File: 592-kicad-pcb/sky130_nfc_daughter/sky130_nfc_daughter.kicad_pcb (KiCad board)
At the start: 4 copper layers, 50 x 52 mm, 154 parts, among them J1 Conn_01x04, J10 U.FL, J11 U.FL, J12 U.FL, J13 U.FL, J2 U.FL, J3 U.FL, J4 U.FL, J5 U.FL, J6 U.FL, J7 U.FL, J8 U.FL, J9 U.FL, U1 Caravel_QFN, U2 24LC02, U3 W25Q32JVZP

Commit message: Add files via upload
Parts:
- removed J1: Conn_01x04, Connector_PinHeader_2.54mm:PinHeader_1x04_P2.54mm_Vertical
- removed J10, J11, J12, J13, J2, J3, J4, J5, J6, J7, J8, J9: U.FL, psysnapeda:SAMTEC_RSP-122811-01
- removed JP10, JP11, JP12, JP5, JP6, JP7, JP8, JP9: Jumper_2_Small_Bridged, Jumper:SolderJumper-2_P1.3mm_Bridged_RoundedPad1.0x1.5mm
- removed R1, R2: 1k, Resistor_SMD:R_0402_1005Metric
- removed R6, R7: 0R, Resistor_SMD:R_0402_1005Metric
- removed U2: 24LC02, Package_DFN_QFN:DFN-8-1EP_3x2mm_P0.5mm_EP1.75x1.45mm
- added JP13: Jumper_2_Small_Bridged, Jumper:SolderJumper-2_P1.3mm_Bridged_RoundedPad1.0x1.5mm, F.Cu at (81.3, 7.10)
- moved JP2 56.4 mm to (81.3, -3.55), turned to 0 degrees
- moved JP4 56.3 mm to (81.3, 3.55), turned to 0 degrees
- moved JP1 54.3 mm to (81.3, -7.10), turned to 0 degrees
- moved JP3 54.3 mm to (81.3, 0.00), turned to 0 degrees
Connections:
- net /hd_an0 renamed /J_ANA_MUX_OUT_EXT
- CON1 pad 36: /clock_uncore -> /J_clock_uncore
- CON1 pad 40: /VRECT_OUT_EXT -> /J_VRECT_OUT_EXT
- CON2 pad 20: /ext_clk_dig -> /J_ext_clk_dig
- CON2 pad 35: /ANA_MUX_OUT_2_EXT -> /J_ANA_MUX_OUT_2_EXT
- CON2 pad 38: /VREF_EXT -> /J_VREF_EXT
- CON2 pad 5: /clk -> /J_clk
- JP1 pad 1: /chip_an0 -> /ANA_MUX_OUT_EXT
- JP2 pad 1: /chip_an1 -> /ext_reset_dig
- JP2 pad 2: /hd_an1 -> /J_ext_clk_dig
- JP3 pad 1: /chip_an2 -> /clk
- JP3 pad 2: /hd_an2 -> /J_clk
- JP4 pad 1: /chip_an3 -> /clock_uncore
- JP4 pad 2: /hd_an3 -> /J_clock_uncore

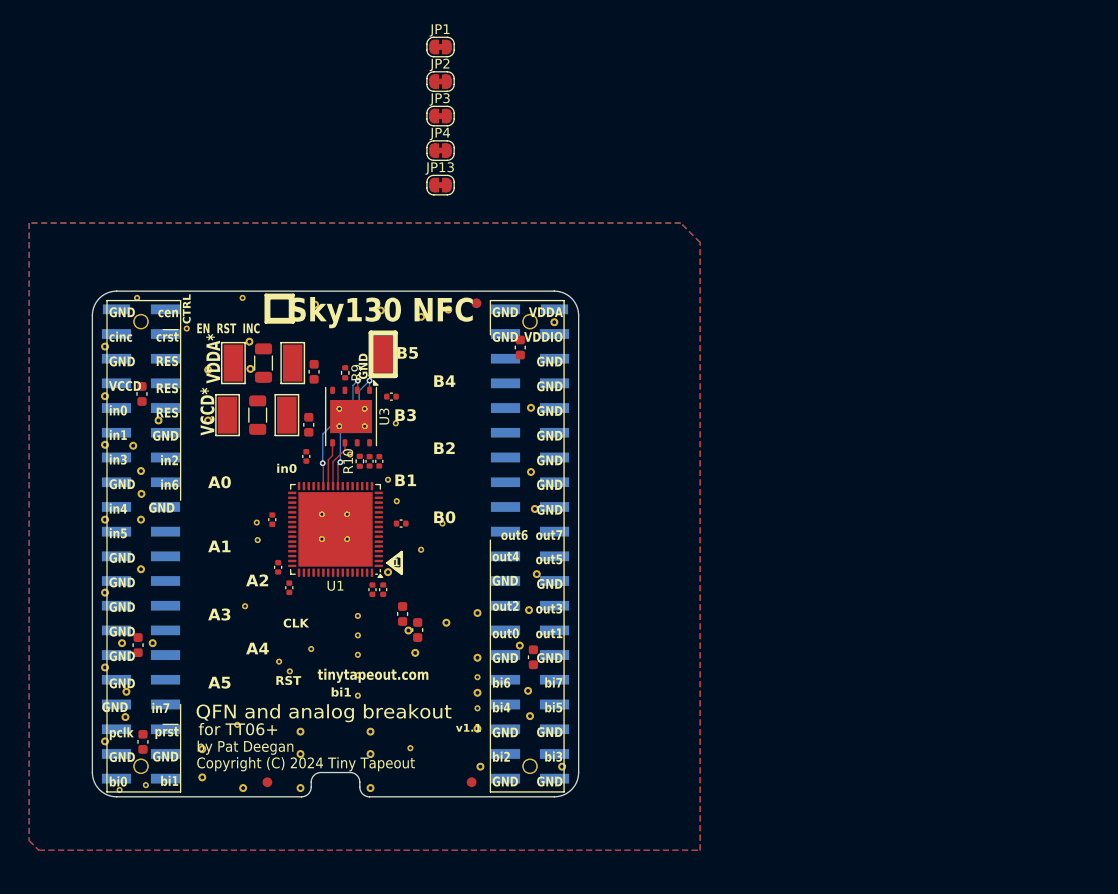
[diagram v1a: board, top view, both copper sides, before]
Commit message: add mezzanine symbol/footprint, init daughterboard placement
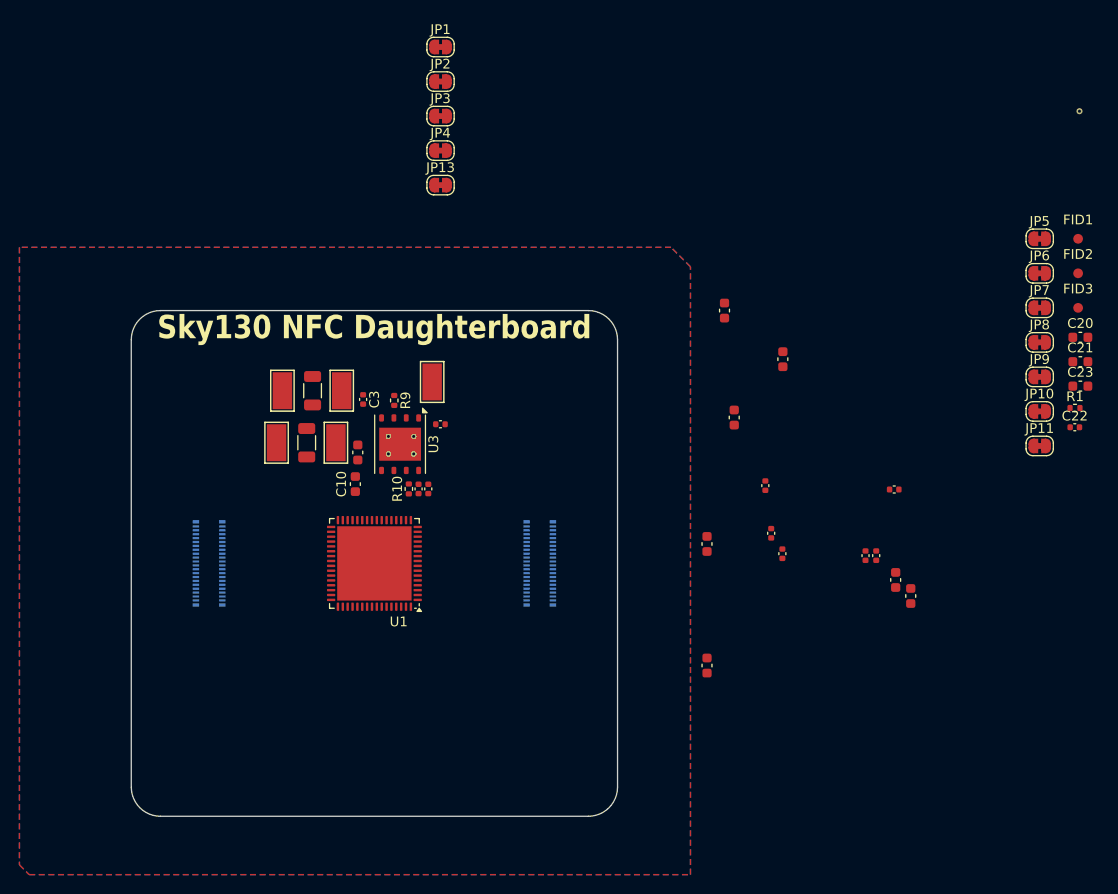
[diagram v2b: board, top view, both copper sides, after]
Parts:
- removed CON1, CON2: ~, TinyTapeout:FH-00148_PinSocket_2x20_P2.54mm
- removed REF**: Z2A_logo, Logos:Z2A_logo
- removed REF**: TT_logo, Logos:TT_logo
- removed STITCHB1 (x53): StitchingVia-0.4mmDrill, flyingcarsfootprints:StitchingVia-0.4mmDrill
- removed the STITCHM1 at (62.4, 41.8)
- removed the STITCHM1 at (78.2, 65.0)
- removed the STITCHM1 at (61.2, 50.4)
- removed the STITCHM1 at (72.8, 51.4)
- removed the STITCHM1 at (69.1, 41.0)
- removed the STITCHM1 at (64.7, 56.1)
- removed the STITCHM1 at (68.0, 54.8)
- removed the STITCHM1 at (55.2, 21.9)
- removed the STITCHM1 at (72.8, 55.4)
- removed the STITCHM1 at (76.8, 39.6)
- removed the STITCHM1 at (51.0, 68.8)
- removed the STITCHM1 at (60.4, 62.6)
- removed the STITCHM1 at (72.8, 53.4)
- removed the STITCHM1 at (65.8, 57.1)
- removed the STITCHM1 at (48.3, 69.3)
- removed the STITCHM1 at (81.5, 41.9)
- removed the STITCHM1 at (61.0, 18.7)
- removed the STITCHM1 at (71.7, 41.0)
- removed the STITCHM1 at (75.9, 37.4)
- removed the STITCHM1 at (62.5, 43.6)
- removed the STITCHM1 at (79.3, 44.6)
- removed the STITCHM1 at (85.1, 57.7)
- removed the STITCHM1 at (71.7, 43.5)
- removed the STITCHM1 at (50.1, 18.7)
- removed the STITCHM1 at (72.0, 34.8)
- removed the STITCHM1 at (72.8, 59.6)
- removed the STITCHM1 at (72.8, 57.5)
- removed the STITCHM1 at (85.1, 60.9)
- removed the STITCHM1 at (69.1, 43.5)
- added C20: C_1u_0603_50V, Capacitor_SMD:C_0603_1608Metric, F.Cu at (147.1, 22.8)
- added C21: C_1u_0603_50V, Capacitor_SMD:C_0603_1608Metric, F.Cu at (147.1, 25.3)
- added C22: 0.1uf, Capacitor_SMD:C_0402_1005Metric, F.Cu at (146.5, 32.0)
- added C23: C_1u_0603_50V, Capacitor_SMD:C_0603_1608Metric, F.Cu at (147.1, 27.8)
- added J8: DF40C-40DS-0.4V_51_, 592-partslib:DF40C40DP04V51, B.Cu at (57.5, 46.0)
- added J9: DF40C-40DS-0.4V_51_, 592-partslib:DF40C40DP04V51, B.Cu at (91.5, 46.0)
- added JP10: Jumper_2_Small_Bridged, Jumper:SolderJumper-2_P1.3mm_Bridged_RoundedPad1.0x1.5mm, F.Cu at (142.9, 30.4)
- added JP11: Jumper_2_Small_Bridged, Jumper:SolderJumper-2_P1.3mm_Bridged_RoundedPad1.0x1.5mm, F.Cu at (142.9, 33.9)
- added JP5: Jumper_2_Small_Bridged, Jumper:SolderJumper-2_P1.3mm_Bridged_RoundedPad1.0x1.5mm, F.Cu at (142.9, 12.6)
- added JP6: Jumper_2_Small_Bridged, Jumper:SolderJumper-2_P1.3mm_Bridged_RoundedPad1.0x1.5mm, F.Cu at (142.9, 16.2)
- added JP7: Jumper_2_Small_Bridged, Jumper:SolderJumper-2_P1.3mm_Bridged_RoundedPad1.0x1.5mm, F.Cu at (142.9, 19.7)
- added JP8: Jumper_2_Small_Bridged, Jumper:SolderJumper-2_P1.3mm_Bridged_RoundedPad1.0x1.5mm, F.Cu at (142.9, 23.3)
- added JP9: Jumper_2_Small_Bridged, Jumper:SolderJumper-2_P1.3mm_Bridged_RoundedPad1.0x1.5mm, F.Cu at (142.9, 26.8)
- added R1: 10k, Resistor_SMD:R_0402_1005Metric, F.Cu at (146.5, 30.0)
- C10: value 0.1uf -> C_1u_0603_50V; footprint Capacitor_SMD:C_0402_1005Metric -> Capacitor_SMD:C_0603_1608Metric
- C3: value C_1u_0603_50V -> 0.1uf; footprint Capacitor_SMD:C_0603_1608Metric -> Capacitor_SMD:C_0402_1005Metric
- moved FID1 100.4 mm to (146.9, 12.6)
- moved FID3 79.2 mm to (146.9, 19.7)
- moved STITCHM1 77.3 mm to (147.0, -0.50)
- moved FID2 61.9 mm to (146.9, 16.2)
- moved C15 60.5 mm to (110.5, 20.0)
- moved C17 59.4 mm to (108.7, 44.0)
- moved C14 58.5 mm to (108.7, 56.5)
- moved C11 50.8 mm to (114.7, 38.0)
- moved C12 50.8 mm to (115.3, 42.9)
- moved C13 50.8 mm to (128.0, 38.4)
- moved C18 50.8 mm to (129.7, 49.4)
- moved C4 50.8 mm to (116.5, 45.0)
- moved C5 50.8 mm to (125.0, 45.2)
- moved C19 50.8 mm to (128.1, 47.7)
- moved C8 50.8 mm to (126.1, 45.2)
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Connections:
- net Net-(U3-~{HOLD}/~{RESET}/IO_{3}) renamed /flash_rstb
- net Net-(U3-~{WP}/IO_{2}) renamed /flash_wpb
- C1 pad 1: vddio -> vddio_vdda_mgmt_3v3
- C10 pad 1: vdda_all -> vccd_mgmt_1v8
- C11 pad 1: vdda_all -> vdda_user_3v3
- C12 pad 1: vdda_all -> vdda_user_3v3
- C13 pad 2: vdda_all -> vdda_user_3v3
- C14 pad 1: vccd_all -> vccd_user_1v8
- C18 pad 1: vccd_all -> vccd_user_1v8
- C19 pad 1: vddio -> vddio_vdda_mgmt_3v3
- C2 pad 1: vccd_all -> vccd_mgmt_1v8
- C3 pad 1: vdda_all -> GND
- C3 pad 2: GND -> vddio_vdda_mgmt_3v3
- C4 pad 2: vccd_all -> vccd_mgmt_1v8
- C5 pad 2: vccd_all -> vccd_user_1v8
- C6 pad 1: vccd_all -> unconnected-(C6-Pad1)
- C7 pad 2: vddio -> vddio_vdda_mgmt_3v3
- C8 pad 2: vddio -> vddio_vdda_mgmt_3v3
- C9 pad 2: vddio -> vddio_vdda_mgmt_3v3
- JP2 pad 1: /ext_reset_dig -> /ANA_MUX_OUT_2_EXT
- JP2 pad 2: /J_ext_clk_dig -> /J_ANA_MUX_OUT_2_EXT
- R10 pad 1: vdda_all -> vddio_vdda_mgmt_3v3
- R9 pad 1: vdda_all -> vddio_vdda_mgmt_3v3
- TP1 pad 1: vdda_all -> vccd_mgmt_1v8
- TP2 pad 1: vccd_all -> vddio_vdda_mgmt_3v3
- TP3 pad 1: vdda_in -> vccd_user_1v8
- TP4 pad 1: vccd_in -> vdda_user_3v3
- U1 pad 17: vddio -> vddio_vdda_mgmt_3v3
- U1 pad 18: vccd_all -> vccd_mgmt_1v8
- U1 pad 30: vdda_all -> vddio_vdda_mgmt_3v3
- U1 pad 40: vdda_all -> vdda_user_3v3
- U1 pad 47: vdda_all -> vdda_user_3v3
- U1 pad 49: vccd_all -> unconnected-(U1-vccd1-Pad49)
- U1 pad 57: /VDD_EXT -> VDD_EXT
- U1 pad 63: vccd_all -> vccd_user_1v8
- U1 pad 64: vddio -> vddio_vdda_mgmt_3v3
- U1 pad 9: vdda_all -> vdda_user_3v3
- U3 pad 8: vdda_all -> vddio_vdda_mgmt_3v3
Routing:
- net /flash_io1: track 13.4 -> 0.00 mm, vias 2 -> 0
- net /flash_csb: track 13.2 -> 0.00 mm, vias 2 -> 0
- net /flash_clk: track 4.95 -> 0.00 mm
- net /flash_io0: track 4.63 -> 0.00 mm
- added copper zone on In1.Cu, net GND
- added copper zone on In2.Cu, net GND
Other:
- outline, holes or cut-outs redrawn
- board text added: "Sky130 NFC Daughterboard"
- board text removed: "1"
- board text removed: "A0"
- board text removed: "A1"
- board text removed: "A2"
- board text removed: "A3"
- board text removed: "A4"
- board text removed: "A5"
- board text removed: "B0"
- board text removed: "B1"
- board text removed: "B2"
- board text removed: "B3"
- board text removed: "B4"
- board text removed: "B5"
- board text removed: "CLK"
- board text removed: "CTRL"
- board text removed: "Copyright (C) 2024 Tiny Tapeout"
- board text removed: "Design by Pat Deegan https://psychogenic.com"
- board text removed: "EN RST INC"
- board text removed: "GND"
- board text removed: "QFN and analog breakout"
- board text removed: "RES"
- board text removed: "RST"
- board text removed: "Sky130 NFC"
- board text removed: "TT06+ QFN breakout v1"
- board text removed: "TinyTapeout designs are packaged together along with a MUX that allows for directing I/O to any selected project, controlled through the cinc, cen and c~{rst} pins. This PCB provides a way to deliver these chips that will sit atop the demo board, but also allows you to easily integrate the ICs into your own projects. For details, see"
- board text removed: "VCCD"
- board text removed: "VCCD*"
- board text removed: "VDDA"
- board text removed: "VDDA*"
- board text removed: "VDDIO"
- board text removed: "bi0"
- board text removed: "bi1"
- board text removed: "bi2"
- board text removed: "bi3"
- board text removed: "bi4"
- board text removed: "bi5"
- board text removed: "bi6"
- board text removed: "bi7"
- board text removed: "by Pat Deegan"
- board text removed: "cen"
- board text removed: "cinc"
- board text removed: "c~{rst}"
- board text removed: "for TT06+"
- board text removed: "github.com/TinyTapeout/breakout-pcb"
- board text removed: "in0"
- board text removed: "in1"
- board text removed: "in2"
- board text removed: "in3"
- board text removed: "in4"
- board text removed: "in5"
- board text removed: "in6"
- board text removed: "in7"
- board text removed: "out0"
- board text removed: "out1"
- board text removed: "out2"
- board text removed: "out3"
- board text removed: "out4"
- board text removed: "out5"
- board text removed: "out6"
- board text removed: "out7"
- board text removed: "pclk"
- board text removed: "p~{rst}"
- board text removed: "tinytapeout.com"
- board text removed: "v1.1"
- board text removed: "zerotoasiccourse.com"

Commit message: daughter placement v1, add 3D models for mezzanine + uFL
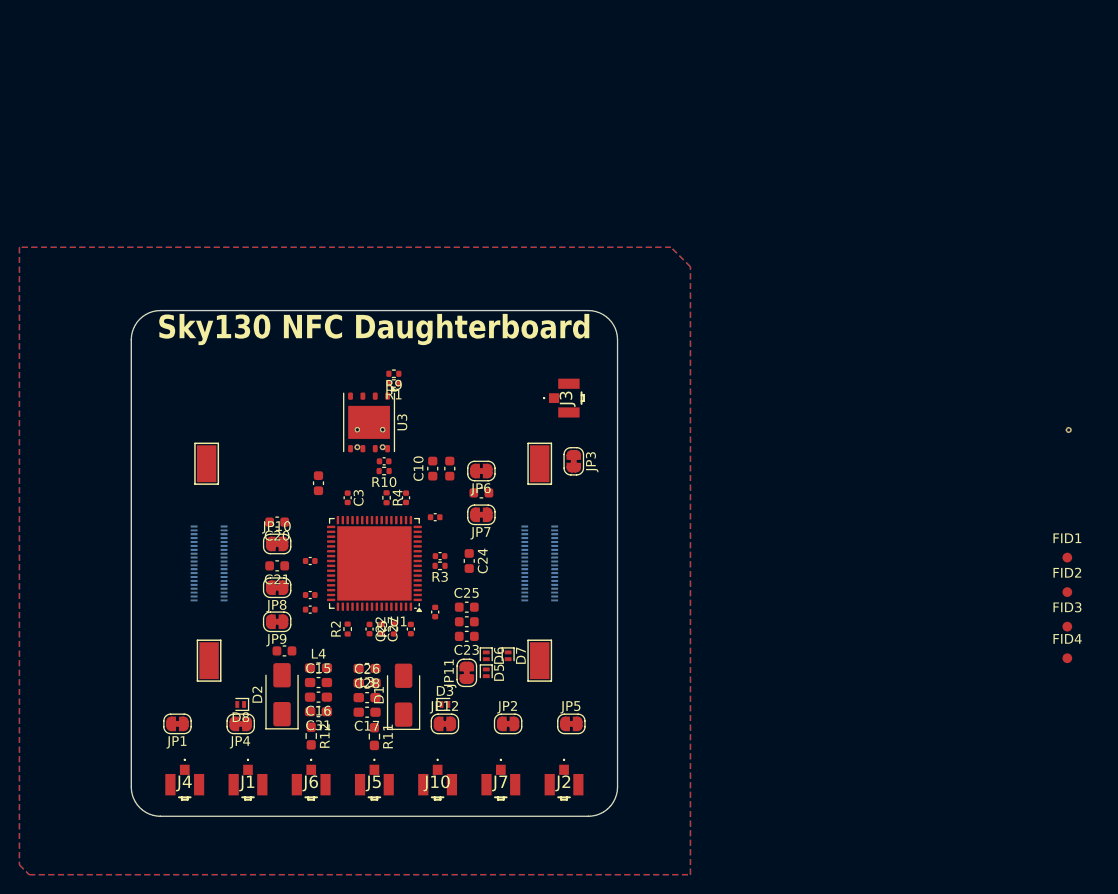
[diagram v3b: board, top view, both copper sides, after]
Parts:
- removed JP13: Jumper_2_Small_Bridged, Jumper:SolderJumper-2_P1.3mm_Bridged_RoundedPad1.0x1.5mm
- removed TP9: TestPoint_Alt, TestPoint:TestPoint_Keystone_5019_Minature
- added C24: C_1u_0603_50V, Capacitor_SMD:C_0603_1608Metric, F.Cu at (84.2, 45.8)
- added C25: C_1u_0603_50V, Capacitor_SMD:C_0603_1608Metric, F.Cu at (84.0, 50.5)
- added C26: C0, Capacitor_SMD:C_0603_1608Metric_Pad1.08x0.95mm_HandSolder, F.Cu at (73.8, 58.3)
- added C27: 0.1uf, Capacitor_SMD:C_0402_1005Metric, F.Cu at (75.2, 52.8)
- added C28: CA, Capacitor_SMD:C_0603_1608Metric_Pad1.08x0.95mm_HandSolder, F.Cu at (73.8, 59.8)
- added C31: CB, Capacitor_SMD:C_0603_1608Metric_Pad1.08x0.95mm_HandSolder, F.Cu at (68.8, 61.2)
- added D1: SMAJ10CA, Diode_SMD:D_SMA, F.Cu at (77.5, 59.5)
- added D2: SMAJ10CA, Diode_SMD:D_SMA, F.Cu at (65.0, 59.5)
- added D3: PESD3V3S1UL, Diode_SMD:D_SOD-882, F.Cu at (81.8, 60.5)
- added D5: PESD3V3S1UL, Diode_SMD:D_SOD-882, F.Cu at (86.0, 57.2)
- added D6: PESD3V3S1UL, Diode_SMD:D_SOD-882, F.Cu at (86.0, 55.5)
- added D7: PESD3V3S1UL, Diode_SMD:D_SOD-882, F.Cu at (88.2, 55.5)
- added D8: PESD3V3S1UL, Diode_SMD:D_SOD-882, F.Cu at (60.8, 60.5)
- added FID4: Fiducial, Fiducial:Fiducial_1mm_Mask2mm, F.Cu at (145.8, 55.8)
- added J1: U.FL-R-SMT-1_80_, 592-partslib:UFLRSMT180, F.Cu at (61.5, 68.8)
- added J10: U.FL-R-SMT-1_80_, 592-partslib:UFLRSMT180, F.Cu at (81.0, 68.8)
- added J2: U.FL-R-SMT-1_80_, 592-partslib:UFLRSMT180, F.Cu at (94.0, 68.8)
- added J3: U.FL-R-SMT-1_80_, 592-partslib:UFLRSMT180, F.Cu at (94.5, 29.0)
- added J4: U.FL-R-SMT-1_80_, 592-partslib:UFLRSMT180, F.Cu at (55.0, 68.8)
- added J5: U.FL-R-SMT-1_80_, 592-partslib:UFLRSMT180, F.Cu at (74.5, 68.8)
- added J6: U.FL-R-SMT-1_80_, 592-partslib:UFLRSMT180, F.Cu at (68.0, 68.8)
- added J7: U.FL-R-SMT-1_80_, 592-partslib:UFLRSMT180, F.Cu at (87.5, 68.8)
- added JP12: Jumper_2_Small_Bridged, Jumper:SolderJumper-2_P1.3mm_Bridged_RoundedPad1.0x1.5mm, F.Cu at (81.8, 62.5)
- added L3: L0, Inductor_SMD:L_0603_1608Metric_Pad1.05x0.95mm_HandSolder, F.Cu at (73.8, 56.8)
- added L4: L0, Inductor_SMD:L_0603_1608Metric_Pad1.05x0.95mm_HandSolder, F.Cu at (68.8, 56.8)
- added R11: Rq, Resistor_SMD:R_0603_1608Metric_Pad0.98x0.95mm_HandSolder, F.Cu at (74.5, 63.8)
- added R12: Rq, Resistor_SMD:R_0603_1608Metric_Pad0.98x0.95mm_HandSolder, F.Cu at (68.0, 63.8)
- added R2: 50, Resistor_SMD:R_0402_1005Metric, F.Cu at (71.8, 52.8)
- added R5: 50, Resistor_SMD:R_0402_1005Metric, F.Cu at (76.5, 52.8)
- C15: value C_1u_0603_50V -> C0; footprint Capacitor_SMD:C_0603_1608Metric -> Capacitor_SMD:C_0603_1608Metric_Pad1.08x0.95mm_HandSolder
- C16: value C_1u_0603_50V -> CA; footprint Capacitor_SMD:C_0603_1608Metric -> Capacitor_SMD:C_0603_1608Metric_Pad1.08x0.95mm_HandSolder
- C17: value C_1u_0603_50V -> CB; footprint Capacitor_SMD:C_0603_1608Metric -> Capacitor_SMD:C_0603_1608Metric_Pad1.08x0.95mm_HandSolder
- J8, J9: footprint 592-partslib:DF40C40DP04V51 -> 592-partslib:DF40C40DS04V51
- R3, R4: value 0R -> 50; footprint Resistor_SMD:R_1206_3216Metric -> Resistor_SMD:R_0402_1005Metric
- moved C21 85.2 mm to (64.5, 46.2), turned to 180 degrees
- moved C20 84.7 mm to (64.5, 41.8), turned to 180 degrees
- moved JP8 82.4 mm to (64.5, 48.5), turned to 180 degrees
- moved JP9 82.4 mm to (64.5, 52.0), turned to 180 degrees
- moved JP10 79.6 mm to (64.5, 44.0)
- moved C22 75.4 mm to (74.0, 52.8), turned to -90 degrees
- moved JP1 74.7 mm to (54.2, 62.5), turned to 180 degrees
- moved R1 70.1 mm to (76.5, 27.5), turned to 180 degrees
- moved JP5 69.3 mm to (94.8, 62.5)
- moved C23 68.1 mm to (84.0, 53.5), turned to 180 degrees
- moved JP2 66.4 mm to (88.2, 62.5)
- moved C18 64.6 mm to (65.2, 55.0), turned to 180 degrees
- moved JP11 63.4 mm to (84.0, 57.2), turned to 90 degrees
- moved JP4 62.4 mm to (60.8, 62.5), turned to 180 degrees
- moved JP7 61.2 mm to (85.5, 41.0), turned to 180 degrees
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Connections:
- C15 pad 1: vdda_all -> GND
- C15 pad 2: GND -> /ANT_NEG_AC_1
- C16 pad 1: vdda_all -> /ANT_NEG_AC_1
- C16 pad 2: GND -> /ANT_NEG_AC_2
- C17 pad 1: vdda_all -> /ANT_POS_AC_2
- C6 pad 1: unconnected-(C6-Pad1) -> vccd_user_1v8
- J8 pad 40: /J_VRECT_OUT_EXT -> /VRECT_OUT_EXT
- J9 pad 32: /FS_EXT -> /J_FS_EXT
- J9 pad 38: /J_VREF_EXT -> /VREF_EXT
- R3 pad 1: vdda_all -> GND
- R3 pad 2: vdda_in -> /ext_clk_dig
- R4 pad 1: vccd_all -> GND
- R4 pad 2: vccd_in -> /clk
- U1 pad 49: unconnected-(U1-vccd1-Pad49) -> vccd_user_1v8
